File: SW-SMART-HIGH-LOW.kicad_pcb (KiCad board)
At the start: 2 copper layers, 72 x 69 mm, 40 parts, among them IC1 MCP1416, J1 SWLINK, J2 USART1, SW1 BTS50010-1TAD, SW2 VNB35N07xx-E, U1 STM32G0B1KBTx, U4 MCP2562-E-SN

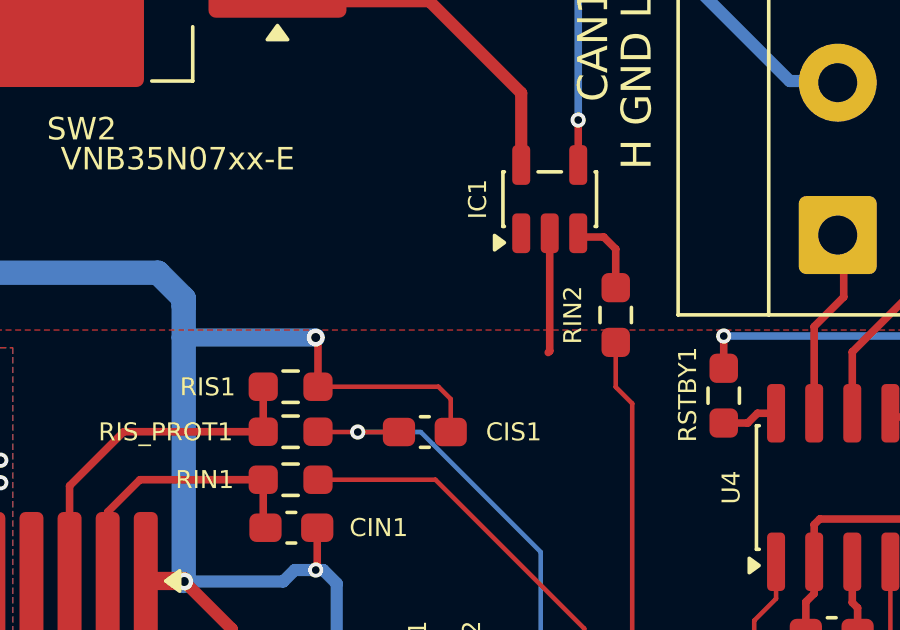
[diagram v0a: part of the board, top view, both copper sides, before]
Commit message: added caps for gate drive IC
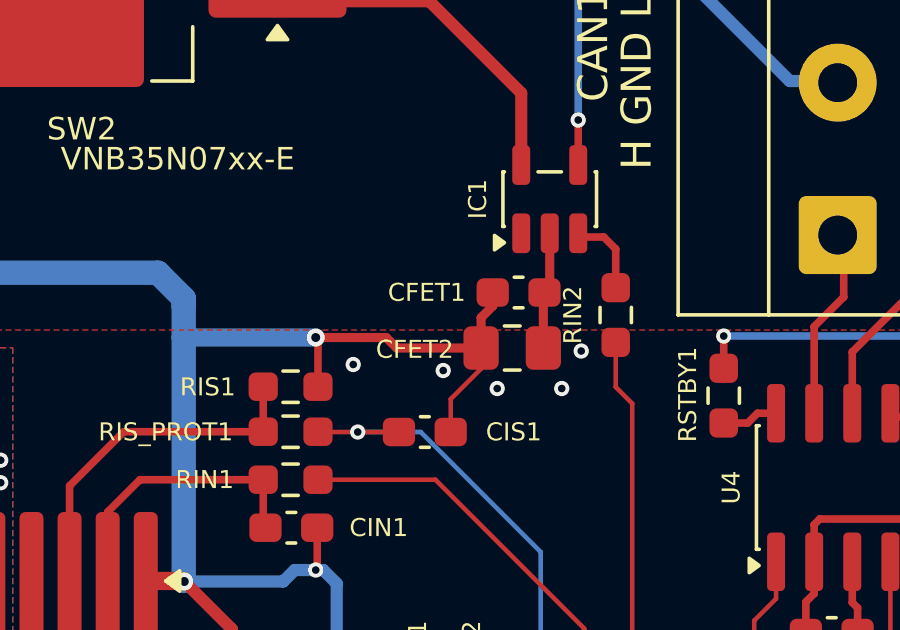
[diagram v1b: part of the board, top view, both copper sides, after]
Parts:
- added CFET1: 100n, Capacitor_SMD:C_0603_1608Metric_Pad1.08x0.95mm_HandSolder, F.Cu at (135.8, 92.2)
- added CFET2: 1u, Capacitor_SMD:C_0805_2012Metric_Pad1.18x1.45mm_HandSolder, F.Cu at (135.6, 94.1)
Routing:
- net GND: track 217.6 -> 222.8 mm
- net +12V: track 17.9 -> 17.8 mm, vias 127 -> 132

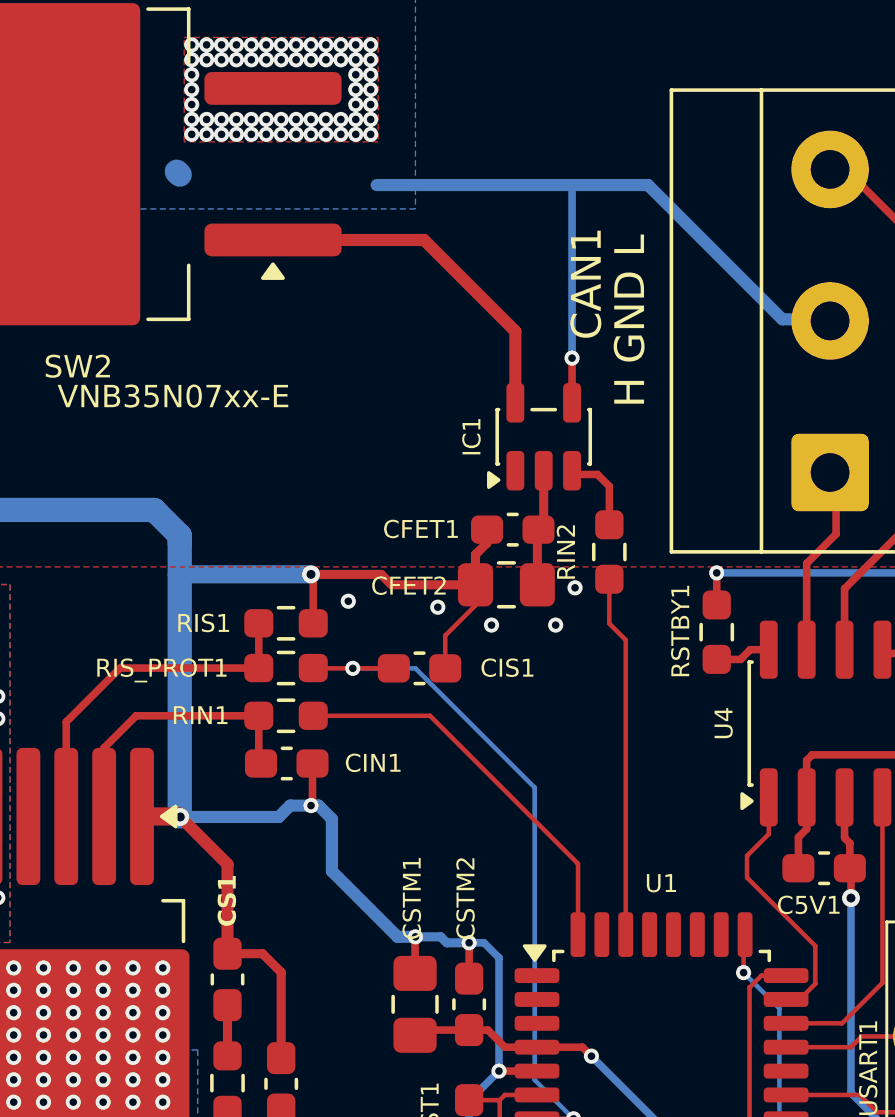
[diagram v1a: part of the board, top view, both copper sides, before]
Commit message: made some tracks wider
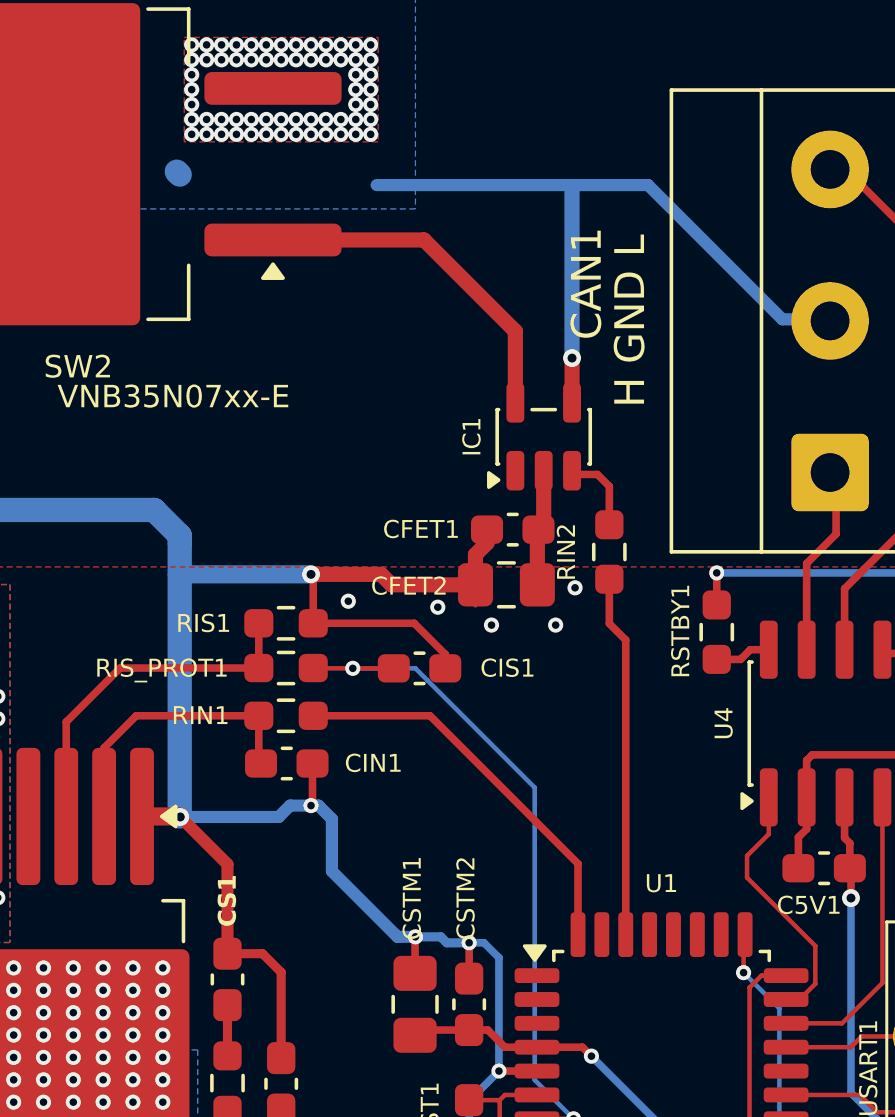
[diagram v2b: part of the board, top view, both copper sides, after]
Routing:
- net GND: track 222.8 -> 225.6 mm
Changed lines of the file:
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@@
 		(start 134.5125 94.1)
 		(end 131.7 94.1)
-		(width 0.305)
+		(width 0.508)
 		(layer "F.Cu")
 		(net 1)
@@
 		(start 134.5125 93.0875)
 		(end 134.5125 94.1)
-		(width 0.305)
+		(width 0.508)
 		(layer "F.Cu")
 		(net 1)
@@
 		(start 134.9 92.7)
 		(end 134.5125 93.0875)
-		(width 0.305)
+		(width 0.508)
+		(layer "F.Cu")
+		(net 1)
+	)
+	(segment
+		(start 133.5 96.9)
+		(end 133.5 96.43)
+		(width 0.254)
 		(layer "F.Cu")
 		(net 1)
@@
 	)
 	(segment
+		(start 132.46 95.39)
+		(end 129.075 95.39)
+		(width 0.254)
+		(layer "F.Cu")
+		(net 1)
+	)
+	(segment
 		(start 115.75 124.84)
 		(end 113.25 124.84)
@@
 	)
 	(segment
-		(start 133.5 95.8)
-		(end 134.5125 94.7875)
-		(width 0.1524)
-		(layer "F.Cu")
-		(net 1)
-	)
-	(segment
 		(start 128.2 119.3)
 		(end 129.3 119.3)
@@
 		(start 131.7 94.1)
 		(end 131.35 93.75)
-		(width 0.305)
-		(layer "F.Cu")
-		(net 1)
-	)
-	(segment
-		(start 133.5 96.9)
-		(end 133.5 95.8)
-		(width 0.1524)
+		(width 0.508)
 		(layer "F.Cu")
 		(net 1)
@@
 		(start 131.35 93.75)
 		(end 129 93.75)
-		(width 0.305)
+		(width 0.508)
+		(layer "F.Cu")
+		(net 1)
+	)
+	(segment
+		(start 133.5 96.43)
+		(end 132.46 95.39)
+		(width 0.254)
 		(layer "F.Cu")
 		(net 1)
@@
 		(start 134.9 92.25)
 		(end 134.9 92.7)
-		(width 0.305)
+		(width 0.508)
 		(layer "F.Cu")
 		(net 1)
@@
 		(start 137.75 88)
 		(end 137.75 86.5)
-		(width 0.254)
+		(width 0.508)
 		(layer "F.Cu")
 		(net 1)
@@
 	(via
 		(at 137.75 86.5)
-		(size 0.508)
-		(drill 0.254)
+		(size 0.6)
+		(drill 0.3)
 		(layers "F.Cu" "B.Cu")
 		(net 1)
@@
 		(start 137.75 86.5)
 		(end 137.75 80.75)
-		(width 0.254)
+		(width 0.508)
 		(layer "B.Cu")
 		(net 1)
@@
 		(start 136.8 90.275)
 		(end 136.8 92.075)
-		(width 0.305)
+		(width 0.508)
 		(layer "F.Cu")
 		(net 4)
@@
 		(start 136.5875 94.1)
 		(end 136.5875 92.2875)
-		(width 0.305)
+		(width 0.508)
 		(layer "F.Cu")
 		(net 4)
@@
 		(start 137.95 103.45)
 		(end 137.95 105.825)
-		(width 0.1524)
+		(width 0.254)
 		(layer "F.Cu")
 		(net 9)
@@
 		(start 129.075 98.49)
 		(end 132.99 98.49)
-		(width 0.1524)
+		(width 0.254)
 		(layer "F.Cu")
 		(net 9)
@@
 		(start 132.99 98.49)
 		(end 137.95 103.45)
-		(width 0.1524)
+		(width 0.254)
 		(layer "F.Cu")
 		(net 9)
@@
 		(start 135.85 85.6)
 		(end 132.79 82.54)
-		(width 0.406)
+		(width 0.508)
 		(layer "F.Cu")
 		(net 10)
@@
 		(start 135.85 88)
 		(end 135.85 85.6)
-		(width 0.406)
+		(width 0.508)
 		(layer "F.Cu")
 		(net 10)
@@
 		(start 132.79 82.54)
 		(end 127.725 82.54)
-		(width 0.406)
+		(width 0.508)
 		(layer "F.Cu")
 		(net 10)
@@
 		(start 139 95.4)
 		(end 139 93.9125)
-		(width 0.1524)
+		(width 0.254)
 		(layer "F.Cu")
 		(net 15)
@@
 		(start 139.55 105.825)
 		(end 139.55 95.95)
-		(width 0.1524)
+		(width 0.254)
 		(layer "F.Cu")
 		(net 15)
@@
 		(start 139.55 95.95)
 		(end 139 95.4)
-		(width 0.1524)
+		(width 0.254)
 		(layer "F.Cu")
 		(net 15)
